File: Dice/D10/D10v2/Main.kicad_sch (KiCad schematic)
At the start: 31 parts, among them J1 Conn_01x14, J2 Conn_01x04, J4 DNP, U1 N52810_QFN32, U2 KXTJ3-1057, Y1 32MHz 40ppm

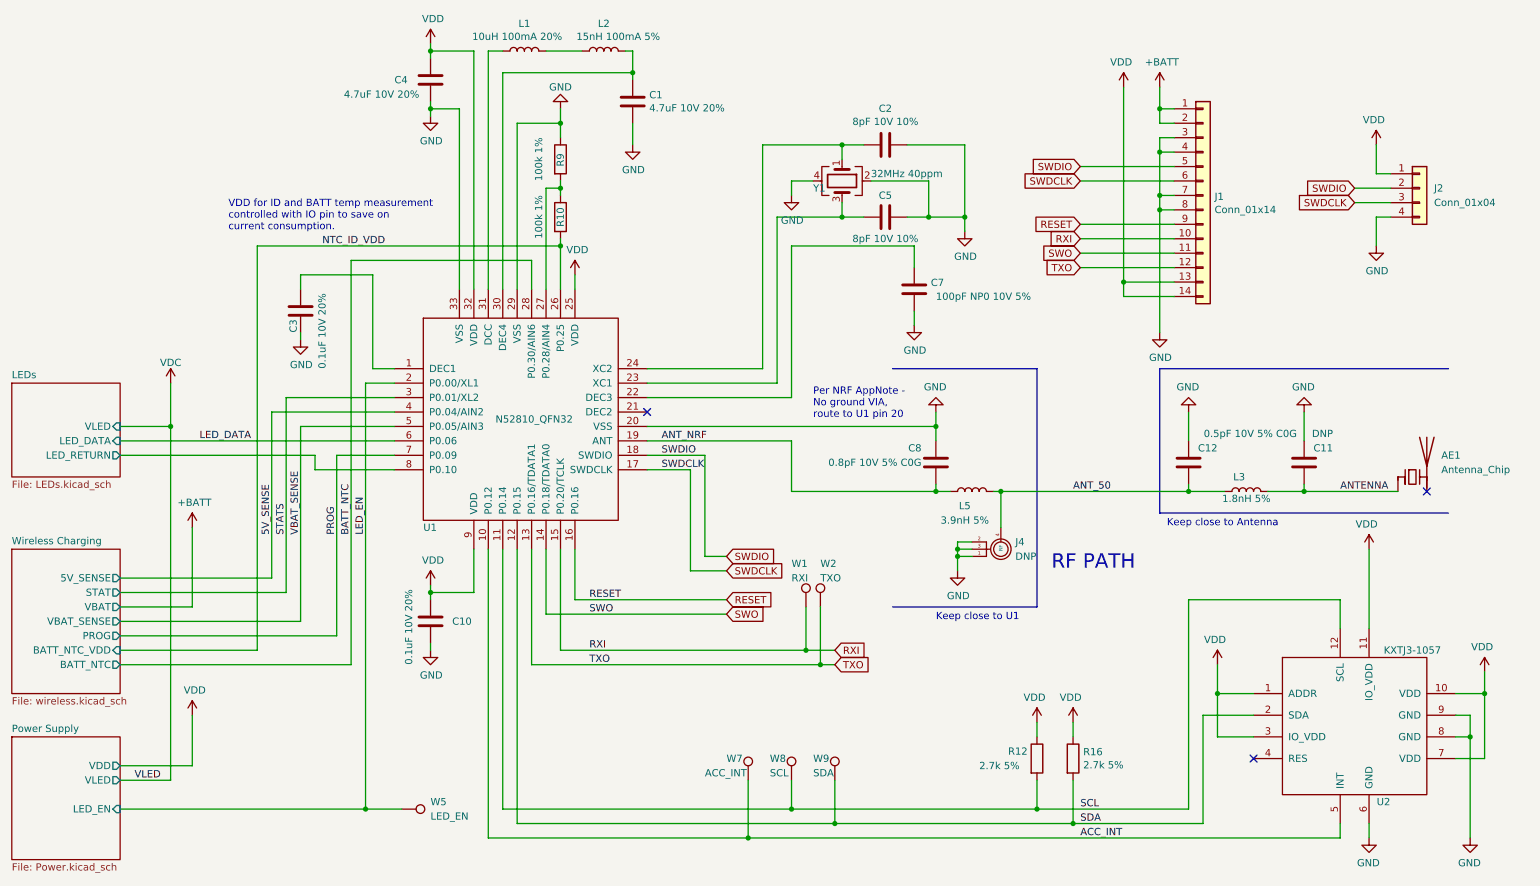
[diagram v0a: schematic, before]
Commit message: Updated all remaining boards to match D20V15 (D6, PD6, D8, D10 and D12)
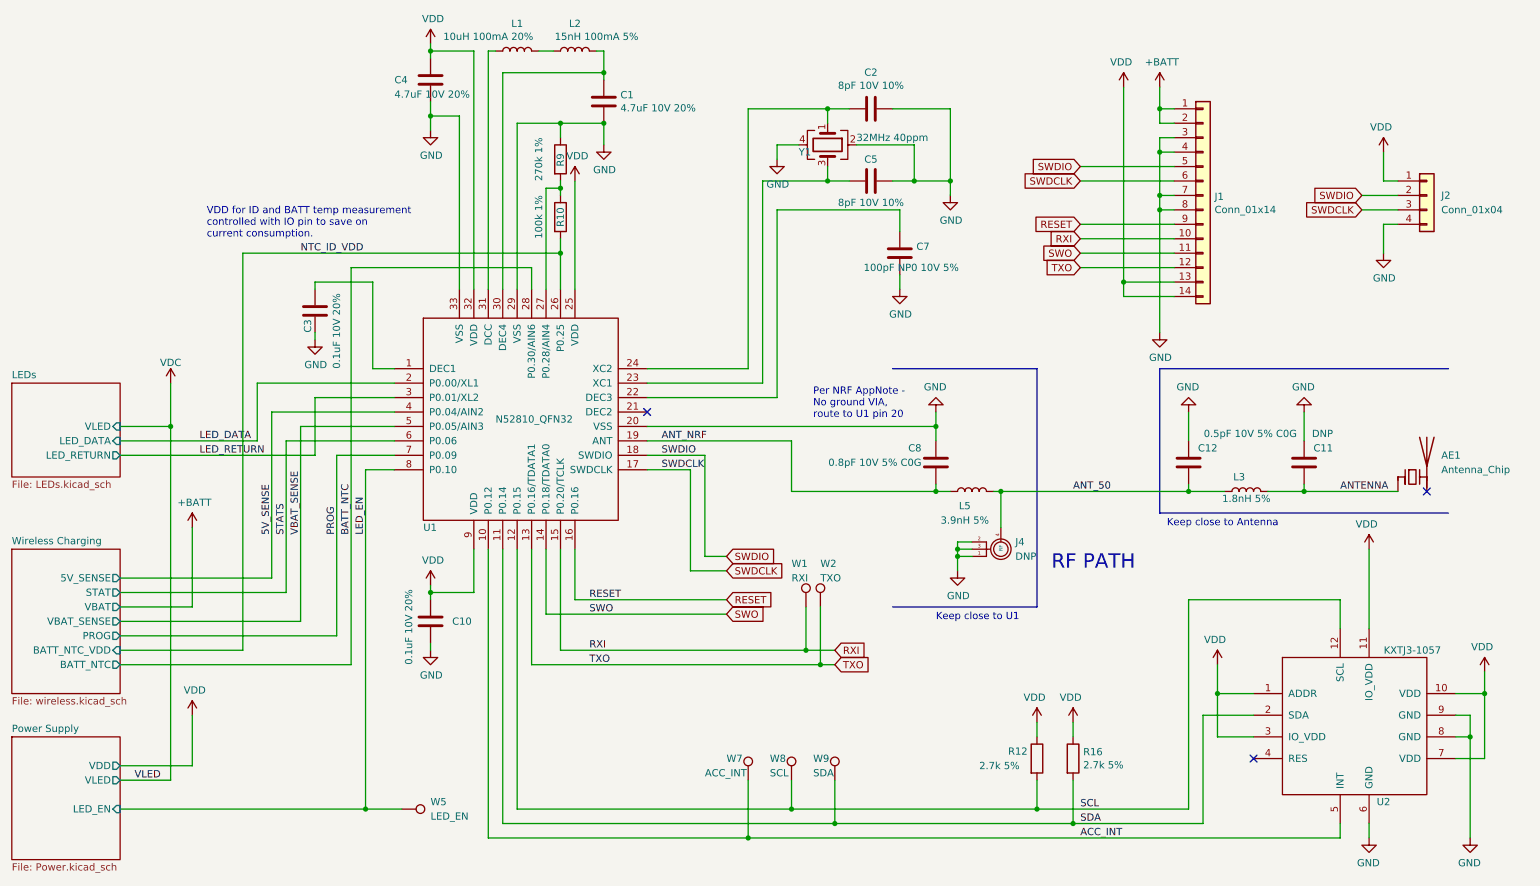
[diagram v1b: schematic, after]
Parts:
- R10, R12, R16: footprint Pixels-dice:R_0402_1005Metric -> Resistor_SMD:R_0402_1005Metric
- R9: value 100k 1% -> 270k 1%; footprint Pixels-dice:R_0402_1005Metric -> Resistor_SMD:R_0402_1005Metric; Manufacturer Part Number 0402WGF1003TCE -> 0402WGF2703TCE
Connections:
- net LEDs/LED_RETURN is gone; now on net LED_EN: U1.8 (P0.10)
- net LED_DATA: now also U1.2 (P0.00/XL1); no longer U1.6 (P0.06)
- net LED_EN: no longer U1.2 (P0.00/XL1)
- net SCL: now also U1.12 (P0.15); no longer U1.11 (P0.14)
- net SDA: now also U1.11 (P0.14); no longer U1.12 (P0.15)
- net STATS: now also U1.6 (P0.06); no longer U1.3 (P0.01/XL2)
- new net LED_RETURN: U1.3 (P0.01/XL2)
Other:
- moved on the sheet: C1, C2, C3, C5, C7, L1, L2, Y1
